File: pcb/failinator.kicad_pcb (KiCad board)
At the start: 2 copper layers, 200 x 124 mm, 68 parts, among them P1 CONN_01X04, P2 CONN_01X06, P3 CONN_01X06, P4 CONN_01X06, U1 74HC594, U2 RASPIPLUSHEADER, U3 LDS-CD16RI, U4 LDS-CD16RI, U5 74HC594

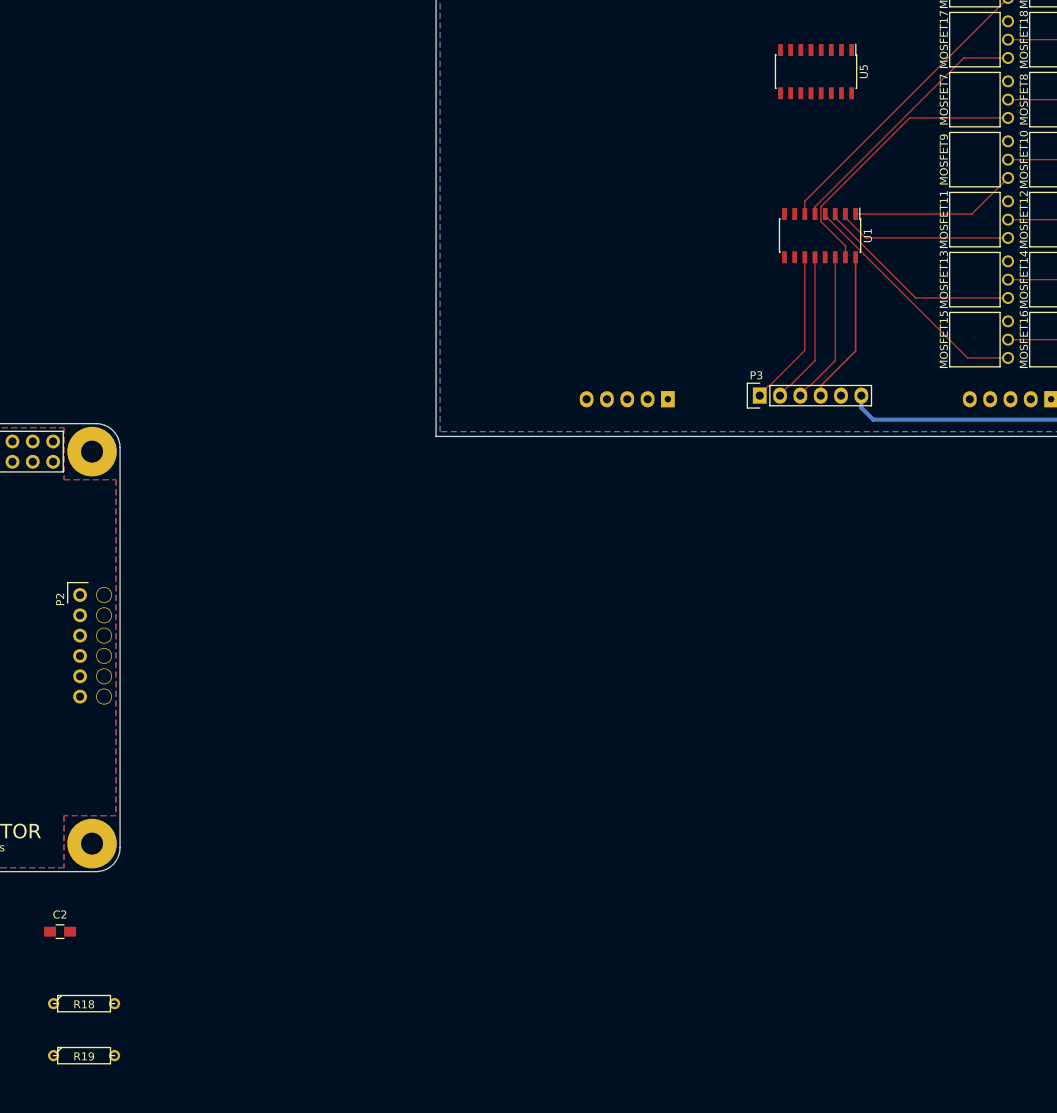
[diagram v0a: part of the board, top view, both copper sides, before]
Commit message: Shift register data connections
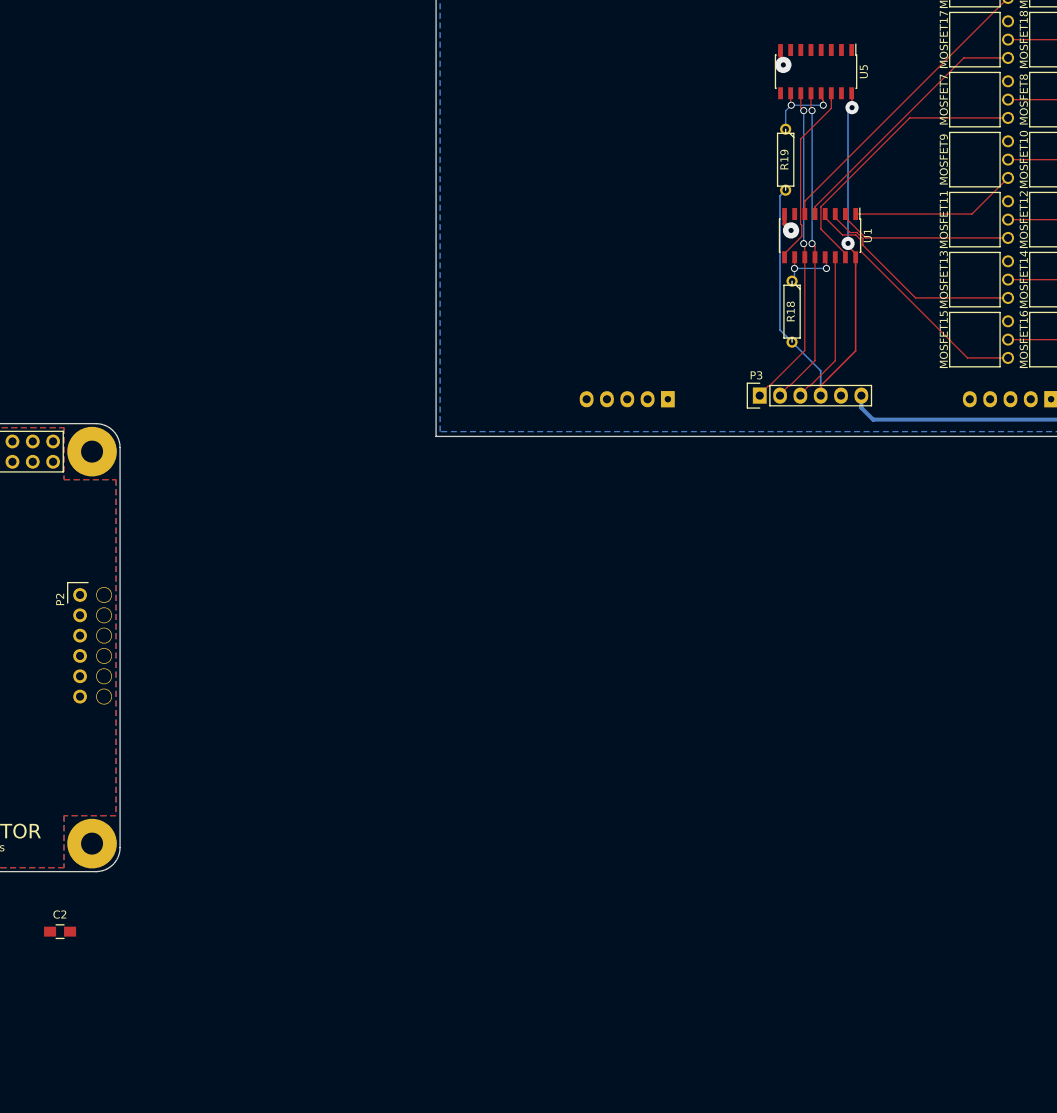
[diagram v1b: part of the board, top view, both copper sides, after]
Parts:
- moved R19 142.2 mm to (243.7, 35.0), turned to 270 degrees
- moved R18 123.8 mm to (244.5, 54.0), turned to 270 degrees
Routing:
- net /D_+3V3: track 19.1 -> 68.3 mm, vias 0 -> 2
- net Net-(U1-Pad9): track 0.00 -> 23.0 mm
- net /D_SCLK: track 19.7 -> 40.4 mm, vias 0 -> 2
- net /D_DISP_CS: track 19.2 -> 39.9 mm, vias 0 -> 2
- net Net-(R19-Pad1): track 0.00 -> 10.4 mm, vias 0 -> 2
- net Net-(R18-Pad1): track 0.00 -> 8.59 mm, vias 0 -> 2
- net /DisplayDrivers/GND: track 0.00 -> 4.41 mm, vias 0 -> 2
- net /DisplayDrivers/E0_L: track 30.4 -> 31.4 mm

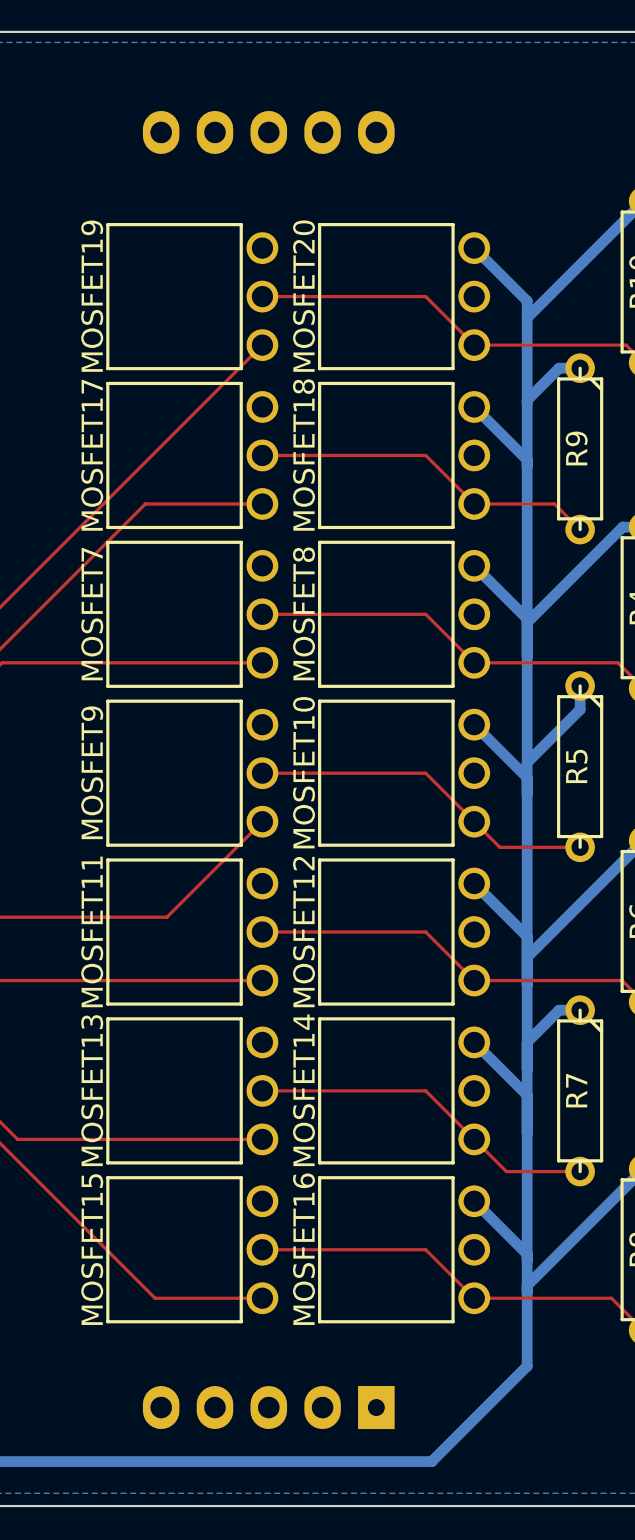
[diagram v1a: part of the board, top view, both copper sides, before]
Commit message: Digit 0 LED segment power traces
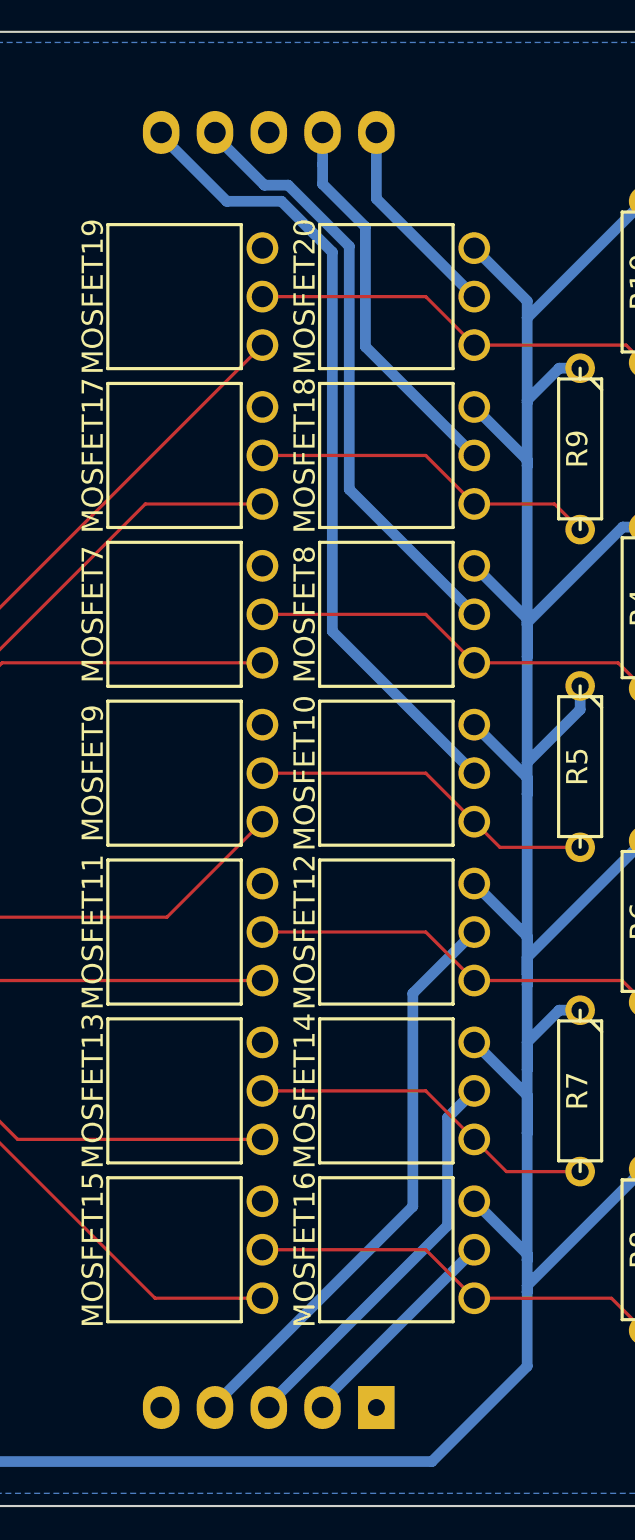
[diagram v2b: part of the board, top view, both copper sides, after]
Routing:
- net /DisplayDrivers/B0_P: track 0.00 -> 37.9 mm
- net /DisplayDrivers/A0_P: track 0.00 -> 28.5 mm
- net /DisplayDrivers/C0_P: track 0.00 -> 27.5 mm
- net /DisplayDrivers/D0_P: track 0.00 -> 19.0 mm
- net /DisplayDrivers/F0_P: track 0.00 -> 18.2 mm
- net /DisplayDrivers/E0_P: track 0.00 -> 10.4 mm
- net /DisplayDrivers/G0_P: track 0.00 -> 9.66 mm
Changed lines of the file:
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@@
     (thickness 1.6)
     (drawings 16)
-    (tracks 290)
+    (tracks 319)
     (zones 0)
     (modules 68)
@@
   (segment (start 271.5 27.5) (end 279.21 27.5) (width 0.1524) (layer F.Cu) (net 41))
   (segment (start 279.21 27.5) (end 281.5 29.79) (width 0.1524) (layer F.Cu) (net 41))
+  (segment (start 272.715635 7.237989) (end 271.595589 7.237989) (width 0.508) (layer B.Cu) (net 42))
+  (segment (start 275.6 10.122354) (end 272.715635 7.237989) (width 0.508) (layer B.Cu) (net 42))
+  (segment (start 275.6 21.6) (end 275.6 10.122354) (width 0.508) (layer B.Cu) (net 42))
+  (segment (start 281.5 27.5) (end 275.6 21.6) (width 0.508) (layer B.Cu) (net 42))
+  (segment (start 269.26 4.9024) (end 269.26 4.75) (width 0.508) (layer B.Cu) (net 42))
+  (segment (start 271.595589 7.237989) (end 269.26 4.9024) (width 0.508) (layer B.Cu) (net 42))
   (segment (start 284 59.5) (end 284 58) (width 0.508) (layer B.Cu) (net 43))
   (segment (start 281.5 55.21) (end 284 57.71) (width 0.508) (layer B.Cu) (net 43))
@@
   (segment (start 271.5 35) (end 279.21 35) (width 0.1524) (layer F.Cu) (net 45))
   (segment (start 279.21 35) (end 281.5 37.29) (width 0.1524) (layer F.Cu) (net 45))
+  (segment (start 272.4 8) (end 269.8176 8) (width 0.508) (layer B.Cu) (net 46))
+  (segment (start 269.8176 8) (end 266.72 4.9024) (width 0.508) (layer B.Cu) (net 46))
+  (segment (start 266.72 4.9024) (end 266.72 4.75) (width 0.508) (layer B.Cu) (net 46))
+  (segment (start 274.8 10.4) (end 272.4 8) (width 0.508) (layer B.Cu) (net 46))
+  (segment (start 281.5 35) (end 274.8 28.3) (width 0.508) (layer B.Cu) (net 46))
+  (segment (start 274.8 28.3) (end 274.8 10.4) (width 0.508) (layer B.Cu) (net 46))
   (segment (start 251.175 41.8) (end 251.175 42.25) (width 0.1524) (layer F.Cu) (net 47))
   (segment (start 251.175 42.25) (end 253.715 44.79) (width 0.1524) (layer F.Cu) (net 47))
@@
   (segment (start 271.5 42.5) (end 279.21 42.5) (width 0.1524) (layer F.Cu) (net 48))
   (segment (start 279.21 42.5) (end 281.5 44.79) (width 0.1524) (layer F.Cu) (net 48))
+  (segment (start 281.5 42.5) (end 278.6 45.4) (width 0.508) (layer B.Cu) (net 49))
+  (segment (start 278.6 45.4) (end 278.6 55.4576) (width 0.508) (layer B.Cu) (net 49))
+  (segment (start 278.6 55.4576) (end 269.26 64.7976) (width 0.508) (layer B.Cu) (net 49))
+  (segment (start 269.26 64.7976) (end 269.26 64.95) (width 0.508) (layer B.Cu) (net 49))
   (segment (start 253.358913 45.703913) (end 259.945 52.29) (width 0.1524) (layer F.Cu) (net 50))
   (segment (start 251.768523 44.113523) (end 252.604662 44.113523) (width 0.1524) (layer F.Cu) (net 50))
@@
   (segment (start 271.5 50) (end 279.21 50) (width 0.1524) (layer F.Cu) (net 51))
   (segment (start 279.21 50) (end 281.5 52.29) (width 0.1524) (layer F.Cu) (net 51))
+  (segment (start 281.5 50) (end 280.241999 51.258001) (width 0.508) (layer B.Cu) (net 52))
+  (segment (start 280.241999 51.258001) (end 280.241999 56.355601) (width 0.508) (layer B.Cu) (net 52))
+  (segment (start 280.241999 56.355601) (end 271.8 64.7976) (width 0.508) (layer B.Cu) (net 52))
+  (segment (start 271.8 64.7976) (end 271.8 64.95) (width 0.508) (layer B.Cu) (net 52))
   (segment (start 253.054102 46.410584) (end 266.433518 59.79) (width 0.1524) (layer F.Cu) (net 53))
   (segment (start 250.803334 44.418334) (end 252.478406 44.418334) (width 0.1524) (layer F.Cu) (net 53))
@@
   (segment (start 271.5 57.5) (end 279.21 57.5) (width 0.1524) (layer F.Cu) (net 54))
   (segment (start 279.21 57.5) (end 281.5 59.79) (width 0.1524) (layer F.Cu) (net 54))
+  (segment (start 281.5 57.5) (end 274.34 64.66) (width 0.508) (layer B.Cu) (net 55))
+  (segment (start 274.34 64.66) (end 274.34 64.95) (width 0.508) (layer B.Cu) (net 55))
   (segment (start 247.365 41.8) (end 247.365 40.8976) (width 0.1524) (layer F.Cu) (net 56))
   (segment (start 247.365 40.8976) (end 265.9726 22.29) (width 0.1524) (layer F.Cu) (net 56))
@@
   (segment (start 271.5 20) (end 279.21 20) (width 0.1524) (layer F.Cu) (net 57))
   (segment (start 279.21 20) (end 281.5 22.29) (width 0.1524) (layer F.Cu) (net 57))
+  (segment (start 274.34 6.274) (end 274.34 4.75) (width 0.508) (layer B.Cu) (net 58))
+  (segment (start 274.34 7.184708) (end 274.34 6.274) (width 0.508) (layer B.Cu) (net 58))
+  (segment (start 276.362011 14.862011) (end 276.362011 9.206719) (width 0.508) (layer B.Cu) (net 58))
+  (segment (start 281.5 20) (end 276.362011 14.862011) (width 0.508) (layer B.Cu) (net 58))
+  (segment (start 276.362011 9.206719) (end 274.34 7.184708) (width 0.508) (layer B.Cu) (net 58))
   (segment (start 246.095 41.8) (end 246.095 40.195) (width 0.1524) (layer F.Cu) (net 59))
   (segment (start 246.095 40.195) (end 271.5 14.79) (width 0.1524) (layer F.Cu) (net 59))
@@
   (segment (start 271.5 12.5) (end 279.21 12.5) (width 0.1524) (layer F.Cu) (net 60))
   (segment (start 279.21 12.5) (end 281.5 14.79) (width 0.1524) (layer F.Cu) (net 60))
+  (segment (start 281.5 12.5) (end 276.88 7.88) (width 0.508) (layer B.Cu) (net 61))
+  (segment (start 276.88 7.88) (end 276.88 4.75) (width 0.508) (layer B.Cu) (net 61))
   (segment (start 245.595 26.7) (end 245.595 28.509533) (width 0.1524) (layer F.Cu) (net 83))
   (segment (start 245.958587 45.5) (end 245.958587 28.87312) (width 0.1524) (layer B.Cu) (net 83))
